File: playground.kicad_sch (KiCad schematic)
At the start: 47 parts, among them IC11 LM3940IMP-3.3_NOPB, IC9 L293DD, J1 67643-2910, J2 Pump, J3 Fan, J4 Valve, J5 Conn_02x05_Counter_Clockwise, J6 MOLEX POWER CONNECTOR, SW1 SW_DIP_x01, U2 ATSAMD21G18A-A, Y1 32.768kHz

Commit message: Updated layout and schem
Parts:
- removed C9: 1u, Capacitor_SMD:C_0805_2012Metric, symbol Device:C
- TP1, TP10, TP11, TP12, TP2, TP3, TP4, TP5, TP6, TP7, TP8, TP9: footprint TestPoint:TestPoint_Pad_D2.0mm -> TestPoint:TestPoint_Pad_D1.0mm
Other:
- note added: "ANA"
- note added: "CORE"
- note added: "IN"
- note added: "IO"
- moved on the sheet: C10, C11
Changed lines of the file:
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@@
 	)
 	(junction
+		(at 128.27 181.61)
+		(diameter 0)
+		(color 0 0 0 0)
+	)
+	(junction
 		(at 82.55 31.75)
 		(diameter 0)
@@
 	)
 	(junction
-		(at 128.27 181.61)
-		(diameter 0)
-		(color 0 0 0 0)
-	)
-	(junction
 		(at 161.29 133.35)
 		(diameter 0)
@@
 	)
 	(junction
+		(at 128.27 168.91)
+		(diameter 0)
+		(color 0 0 0 0)
+	)
+	(junction
 		(at 95.25 181.61)
 		(diameter 0)
@@
 	)
 	(junction
-		(at 138.43 168.91)
-		(diameter 0)
-		(color 0 0 0 0)
-	)
-	(junction
-		(at 138.43 181.61)
-		(diameter 0)
-		(color 0 0 0 0)
-	)
-	(junction
 		(at 49.53 52.07)
 		(diameter 0)
@@
 		(color 0 0 0 0)
 	)
-	(junction
-		(at 128.27 168.91)
-		(diameter 0)
-		(color 0 0 0 0)
-	)
 	(no_connect
 		(at 207.01 77.47)
@@
 	(wire
 		(pts
-			(xy 138.43 181.61) (xy 149.86 181.61)
+			(xy 128.27 181.61) (xy 139.7 181.61)
 		)
 		(stroke
@@
 	(wire
 		(pts
-			(xy 138.43 168.91) (xy 138.43 171.45)
+			(xy 128.27 168.91) (xy 128.27 171.45)
 		)
 		(stroke
@@
 	(wire
 		(pts
-			(xy 149.86 168.91) (xy 149.86 171.45)
+			(xy 139.7 168.91) (xy 139.7 171.45)
 		)
 		(stroke
@@
 	(wire
 		(pts
-			(xy 128.27 168.91) (xy 138.43 168.91)
-		)
-		(stroke
-			(width 0)
-			(type default)
-		)
-	)
-	(wire
-		(pts
 			(xy 118.11 168.91) (xy 128.27 168.91)
 		)
@@
 	(wire
 		(pts
-			(xy 128.27 181.61) (xy 138.43 181.61)
-		)
-		(stroke
-			(width 0)
-			(type default)
-		)
-	)
-	(wire
-		(pts
 			(xy 144.78 99.06) (xy 144.78 88.9)
 		)
@@
 	(wire
 		(pts
-			(xy 149.86 179.07) (xy 149.86 181.61)
+			(xy 139.7 179.07) (xy 139.7 181.61)
 		)
 		(stroke
@@
 	(wire
 		(pts
-			(xy 128.27 171.45) (xy 128.27 168.91)
-		)
-		(stroke
-			(width 0)
-			(type default)
-		)
-	)
-	(wire
-		(pts
 			(xy 143.51 36.83) (xy 146.05 36.83)
 		)
@@
 	(wire
 		(pts
-			(xy 138.43 179.07) (xy 138.43 181.61)
+			(xy 128.27 179.07) (xy 128.27 181.61)
 		)
 		(stroke
@@
 	(wire
 		(pts
-			(xy 128.27 179.07) (xy 128.27 181.61)
-		)
-		(stroke
-			(width 0)
-			(type default)
-		)
-	)
-	(wire
-		(pts
 			(xy 138.43 81.28) (xy 147.32 81.28)
 		)
@@
 	(wire
 		(pts
-			(xy 138.43 168.91) (xy 149.86 168.91)
+			(xy 128.27 168.91) (xy 139.7 168.91)
 		)
 		(stroke
@@
 		)
 	)
+	(text "IO"
+		(exclude_from_sim no)
+		(at 95.25 167.64 0)
+		(effects
+			(font
+				(size 1.27 1.27)
+			)
+		)
+	)
 	(text "Valve Controller"
 		(exclude_from_sim no)
@@
 		)
 	)
+	(text "ANA"
+		(exclude_from_sim no)
+		(at 139.192 167.132 0)
+		(effects
+			(font
+				(size 1.27 1.27)
+			)
+		)
+	)
 	(text "MOLEX POWER"
 		(exclude_from_sim no)
@@
 		)
 	)
+	(text "ANA"
+		(exclude_from_sim no)
+		(at 86.868 167.64 0)
+		(effects
+			(font
+				(size 1.27 1.27)
+			)
+		)
+	)
 	(text "(NOTE: might modify this)"
 		(exclude_from_sim no)
@@
 		)
 	)
+	(text "IN"
+		(exclude_from_sim no)
+		(at 106.68 167.386 0)
+		(effects
+			(font
+				(size 1.27 1.27)
+			)
+		)
+	)
 	(text "Level Shifter"
 		(exclude_from_sim no)
@@
 		)
 	)
+	(text "IN"
+		(exclude_from_sim no)
+		(at 128.27 167.132 0)
+		(effects
+			(font
+				(size 1.27 1.27)
+			)
+		)
+	)
+	(text "CORE"
+		(exclude_from_sim no)
+		(at 118.11 167.386 0)
+		(effects
+			(font
+				(size 1.27 1.27)
+			)
+		)
+	)
 	(label "SWDIO"
 		(at 25.4 168.91 0)
@@
 			)
 		)
-		(property "Footprint" "TestPoint:TestPoint_Pad_D2.0mm"
+		(property "Footprint" "TestPoint:TestPoint_Pad_D1.0mm"
 			(at 257.81 83.82 0)
 			(effects
@@
 			)
 		)
-		(property "Footprint" "TestPoint:TestPoint_Pad_D2.0mm"
+		(property "Footprint" "TestPoint:TestPoint_Pad_D1.0mm"
 			(at 255.27 62.23 0)
 			(effects
@@
 			)
 		)
-		(property "Footprint" "TestPoint:TestPoint_Pad_D2.0mm"
+		(property "Footprint" "TestPoint:TestPoint_Pad_D1.0mm"
 			(at 257.81 91.44 0)
 			(effects
@@
 			)
 		)
-		(property "Footprint" "TestPoint:TestPoint_Pad_D2.0mm"
+		(property "Footprint" "TestPoint:TestPoint_Pad_D1.0mm"
 			(at 257.81 78.74 0)
 			(effects
@@
 			)
 		)
-		(property "Footprint" "TestPoint:TestPoint_Pad_D2.0mm"
+		(property "Footprint" "TestPoint:TestPoint_Pad_D1.0mm"
 			(at 257.81 76.2 0)
 			(effects
@@
 			)
 		)
-		(property "Footprint" "TestPoint:TestPoint_Pad_D2.0mm"
+		(property "Footprint" "TestPoint:TestPoint_Pad_D1.0mm"
 			(at 257.81 93.98 0)
 			(effects
@@
 			)
 		)
-		(property "Footprint" "TestPoint:TestPoint_Pad_D2.0mm"
+		(property "Footprint" "TestPoint:TestPoint_Pad_D1.0mm"
 			(at 257.81 88.9 0)
 			(effects
@@
 			)
 		)
-		(property "Footprint" "TestPoint:TestPoint_Pad_D2.0mm"
+		(property "Footprint" "TestPoint:TestPoint_Pad_D1.0mm"
 			(at 247.65 62.23 0)
 			(effects
@@
 			)
 		)
-		(property "Footprint" "TestPoint:TestPoint_Pad_D2.0mm"
+		(property "Footprint" "TestPoint:TestPoint_Pad_D1.0mm"
 			(at 240.03 62.23 0)
 			(effects
@@
 	(symbol
 		(lib_id "Device:C")
-		(at 138.43 175.26 0)
+		(at 128.27 175.26 0)
 		(unit 1)
 		(exclude_from_sim no)
@@
 		(fields_autoplaced yes)
 		(property "Reference" "C10"
-			(at 142.24 173.9899 0)
+			(at 132.08 173.9899 0)
 			(effects
 				(font
@@
 		)
 		(property "Value" "10u"
-			(at 142.24 176.5299 0)
+			(at 132.08 176.5299 0)
 			(effects
 				(font
@@
 		)
 		(property "Footprint" "Capacitor_SMD:C_0805_2012Metric"
-			(at 139.3952 179.07 0)
+			(at 129.2352 179.07 0)
 			(effects
 				(font
@@
 		)
 		(property "Datasheet" "~"
-			(at 138.43 175.26 0)
+			(at 128.27 175.26 0)
 			(effects
 				(font
@@
 		)
 		(property "Description" "Unpolarized capacitor"
-			(at 138.43 175.26 0)
+			(at 128.27 175.26 0)
 			(effects
 				(font
@@
 	(symbol
 		(lib_id "Device:C")
-		(at 149.86 175.26 0)
+		(at 139.7 175.26 0)
 		(unit 1)
 		(exclude_from_sim no)
@@
 		(fields_autoplaced yes)
 		(property "Reference" "C11"
-			(at 153.67 173.9899 0)
+			(at 143.51 173.9899 0)
 			(effects
 				(font
@@
 		)
 		(property "Value" "10u"
-			(at 153.67 176.5299 0)
+			(at 143.51 176.5299 0)
 			(effects
 				(font
@@
 		)
 		(property "Footprint" "Capacitor_SMD:C_0805_2012Metric"
-			(at 150.8252 179.07 0)
+			(at 140.6652 179.07 0)
 			(effects
 				(font
@@
 		)
 		(property "Datasheet" "~"
-			(at 149.86 175.26 0)
+			(at 139.7 175.26 0)
 			(effects
 				(font
@@
 		)
 		(property "Description" "Unpolarized capacitor"
-			(at 149.86 175.26 0)
+			(at 139.7 175.26 0)
 			(effects
 				(font
@@
 	)
 	(symbol
-		(lib_id "Device:C")
-		(at 128.27 175.26 0)
-		(unit 1)
-		(exclude_from_sim no)
-		(in_bom yes)
-		(on_board yes)
-		(dnp no)
-		(fields_autoplaced yes)
-		(property "Reference" "C9"
-			(at 132.08 173.9899 0)
-			(effects
-				(font
-					(size 1.27 1.27)
-				)
-				(justify left)
-			)
-		)
-		(property "Value" "1u"
-			(at 132.08 176.5299 0)
-			(effects
-				(font
-					(size 1.27 1.27)
-				)
-				(justify left)
-			)
-		)
-		(property "Footprint" "Capacitor_SMD:C_0805_2012Metric"
-			(at 129.2352 179.07 0)
-			(effects
-				(font
-					(size 1.27 1.27)
-				)
-				(hide yes)
-			)
-		)
-		(property "Datasheet" "~"
-			(at 128.27 175.26 0)
-			(effects
-				(font
-					(size 1.27 1.27)
-				)
-				(hide yes)
-			)
-		)
-		(property "Description" "Unpolarized capacitor"
-			(at 128.27 175.26 0)
-			(effects
-				(font
-					(size 1.27 1.27)
-				)
-				(hide yes)
-			)
-		)
-		(pin "1"
-		)
-		(pin "2"
-		)
-		(instances
-			(project "playground"
-				(path "/e7dc7c2b-347f-4a52-91f1-4651868a2780"
-					(reference "C9")
-					(unit 1)
-				)
-			)
-		)
-	)
-	(symbol
 		(lib_id "power:+3V3")
 		(at 83.82 168.91 0)
@@
 			)
 		)
-		(property "Footprint" "TestPoint:TestPoint_Pad_D2.0mm"
+		(property "Footprint" "TestPoint:TestPoint_Pad_D1.0mm"
 			(at 262.89 62.23 0)
 			(effects
@@
 			)
 		)
-		(property "Footprint" "TestPoint:TestPoint_Pad_D2.0mm"
+		(property "Footprint" "TestPoint:TestPoint_Pad_D1.0mm"
 			(at 257.81 86.36 0)
 			(effects
@@
 			)
 		)
-		(property "Footprint" "TestPoint:TestPoint_Pad_D2.0mm"
+		(property "Footprint" "TestPoint:TestPoint_Pad_D1.0mm"
 			(at 257.81 81.28 0)
 			(effects

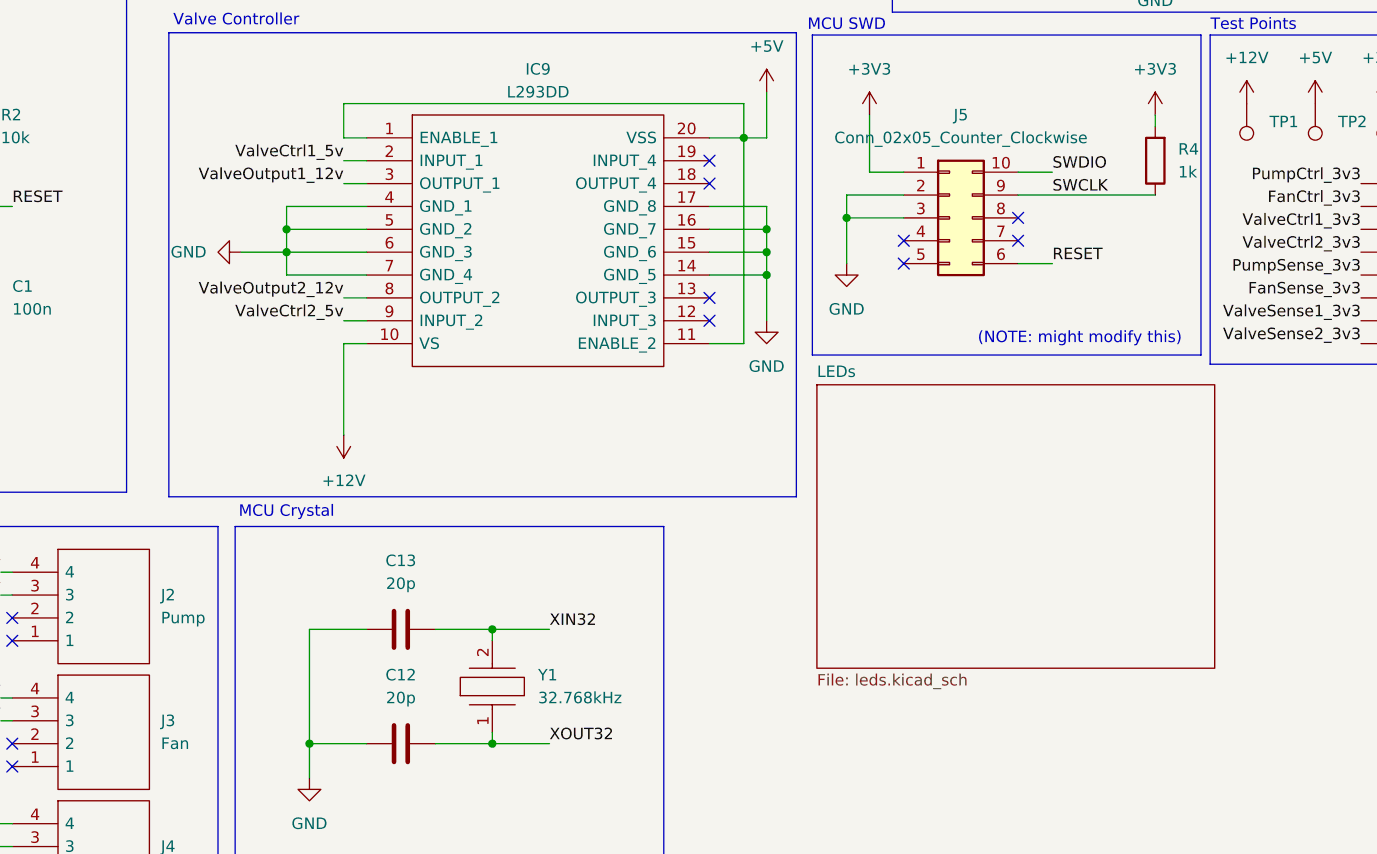
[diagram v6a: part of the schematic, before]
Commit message: Layout of indicator LEDs. Shrank design space
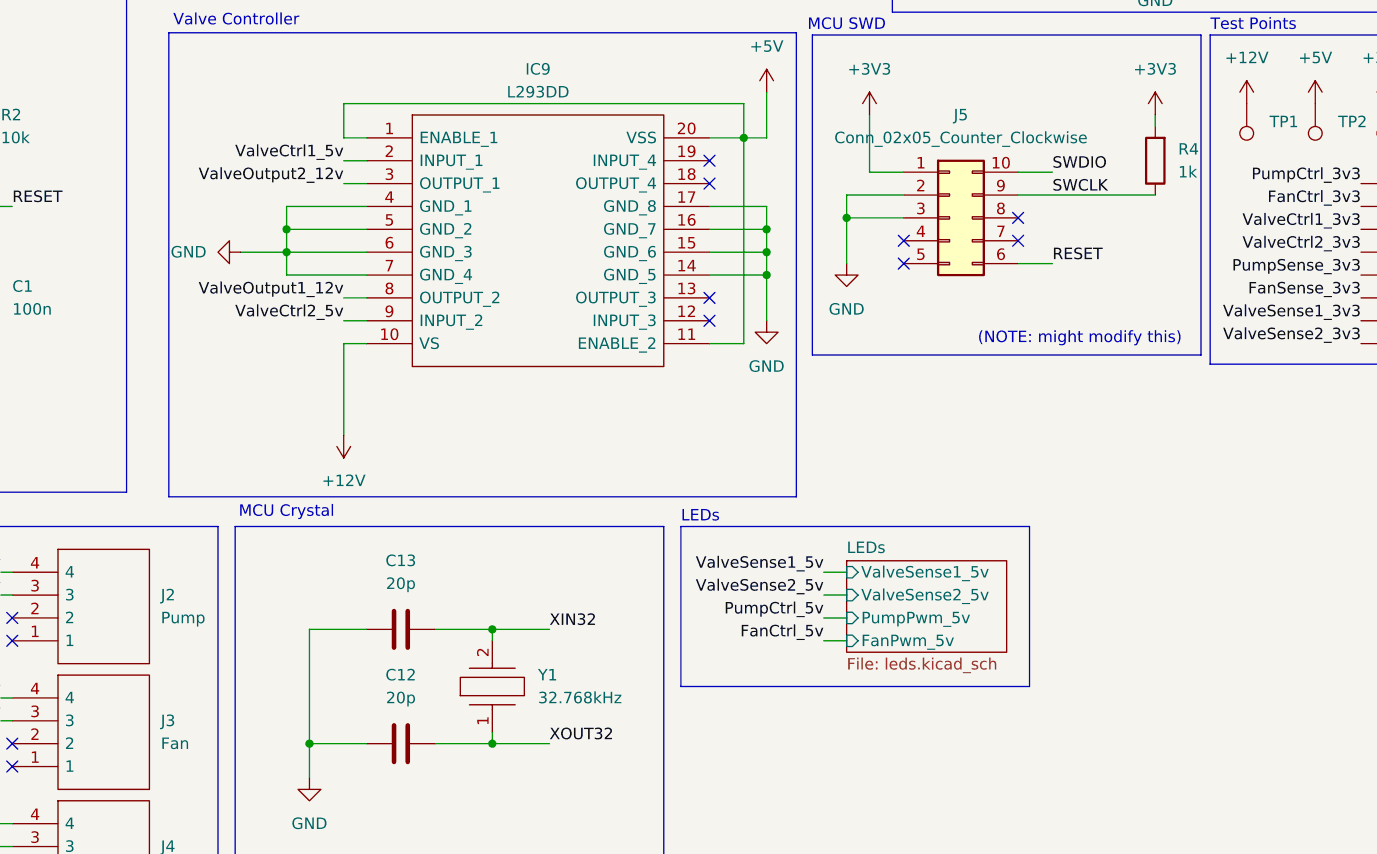
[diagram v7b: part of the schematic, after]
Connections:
- net ValveOutput1_12v: now also IC9.8 (OUTPUT_2); no longer IC9.3 (OUTPUT_1)
- net ValveOutput2_12v: now also IC9.3 (OUTPUT_1); no longer IC9.8 (OUTPUT_2)
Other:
- sheet LEDs ports: added FanPwm_5v, PumpPwm_5v, ValveSense1_5v, ValveSense2_5v; removed none
- note added: "LEDs"
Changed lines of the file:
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@@
 	(wire
 		(pts
+			(xy 198.12 114.3) (xy 200.66 114.3)
+		)
+		(stroke
+			(width 0)
+			(type default)
+		)
+	)
+	(wire
+		(pts
 			(xy 105.41 147.32) (xy 107.95 147.32)
 		)
@@
 	(wire
 		(pts
+			(xy 198.12 116.84) (xy 200.66 116.84)
+		)
+		(stroke
+			(width 0)
+			(type default)
+		)
+	)
+	(wire
+		(pts
 			(xy 17.78 173.99) (xy 35.56 173.99)
 		)
@@
 	(wire
 		(pts
+			(xy 198.12 121.92) (xy 200.66 121.92)
+		)
+		(stroke
+			(width 0)
+			(type default)
+		)
+	)
+	(wire
+		(pts
 			(xy 106.68 130.81) (xy 107.95 130.81)
 		)
@@
 	(wire
 		(pts
+			(xy 198.12 119.38) (xy 200.66 119.38)
+		)
+		(stroke
+			(width 0)
+			(type default)
+		)
+	)
+	(wire
+		(pts
 			(xy 144.78 68.58) (xy 147.32 68.58)
 		)
@@
 	)
 	(rectangle
+		(start 182.245 109.22)
+		(end 220.98 127)
+		(stroke
+			(width 0)
+			(type default)
+		)
+		(fill
+			(type none)
+		)
+	)
+	(rectangle
 		(start 125.476 15.748)
 		(end 204.216 49.784)
@@
 		)
 	)
+	(text "LEDs"
+		(exclude_from_sim no)
+		(at 184.404 108.204 0)
+		(effects
+			(font
+				(size 1.27 1.27)
+			)
+		)
+	)
 	(text "Valve Controller"
 		(exclude_from_sim no)
@@
 		)
 	)
+	(label "ValveSense2_5v"
+		(at 198.12 116.84 180)
+		(fields_autoplaced yes)
+		(effects
+			(font
+				(size 1.27 1.27)
+			)
+			(justify right bottom)
+		)
+	)
 	(label "USB_D+"
 		(at 68.58 39.37 0)
@@
 		)
 	)
+	(label "PumpCtrl_5v"
+		(at 198.12 119.38 180)
+		(fields_autoplaced yes)
+		(effects
+			(font
+				(size 1.27 1.27)
+			)
+			(justify right bottom)
+		)
+	)
 	(label "ValveSense2_5v"
 		(at 105.41 149.86 180)
@@
 		)
 	)
+	(label "ValveSense1_5v"
+		(at 198.12 114.3 180)
+		(fields_autoplaced yes)
+		(effects
+			(font
+				(size 1.27 1.27)
+			)
+			(justify right bottom)
+		)
+	)
 	(label "XIN32"
 		(at 24.13 90.17 0)
@@
 	)
 	(label "ValveOutput2_12v"
-		(at 144.78 83.82 180)
+		(at 144.78 71.12 180)
 		(fields_autoplaced yes)
 		(effects
@@
 		)
 	)
+	(label "FanCtrl_5v"
+		(at 198.12 121.92 180)
+		(fields_autoplaced yes)
+		(effects
+			(font
+				(size 1.27 1.27)
+			)
+			(justify right bottom)
+		)
+	)
 	(label "ValveOutput1_12v"
-		(at 144.78 71.12 180)
+		(at 144.78 83.82 180)
 		(fields_autoplaced yes)
 		(effects
@@
 	)
 	(sheet
-		(at 197.358 93.472)
-		(size 44.196 31.496)
+		(at 200.66 113.03)
+		(size 17.78 10.16)
 		(fields_autoplaced yes)
 		(stroke
@@
 		)
 		(property "Sheetname" "LEDs"
-			(at 197.358 92.7604 0)
+			(at 200.66 112.3184 0)
 			(effects
 				(font
@@
 		)
 		(property "Sheetfile" "leds.kicad_sch"
-			(at 197.358 125.5526 0)
+			(at 200.66 123.7746 0)
 			(effects
 				(font
@@
 			)
 		)
+		(pin "ValveSense1_5v" input
+			(at 200.66 114.3 180)
+			(effects
+				(font
+					(size 1.27 1.27)
+				)
+				(justify left)
+			)
+		)
+		(pin "ValveSense2_5v" input
+			(at 200.66 116.84 180)
+			(effects
+				(font
+					(size 1.27 1.27)
+				)
+				(justify left)
+			)
+		)
+		(pin "PumpPwm_5v" input
+			(at 200.66 119.38 180)
+			(effects
+				(font
+					(size 1.27 1.27)
+				)
+				(justify left)
+			)
+		)
+		(pin "FanPwm_5v" input
+			(at 200.66 121.92 180)
+			(effects
+				(font
+					(size 1.27 1.27)
+				)
+				(justify left)
+			)
+		)

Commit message: Initial Layout
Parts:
- added H1, H2, H3, H4: MountingHole_Pad, MountingHole:MountingHole_2.2mm_M2_Pad, symbol Mechanical:MountingHole_Pad
- J5: footprint Connector_PinHeader_2.54mm:PinHeader_2x05_P2.54mm_Vertical_SMD -> Connector_PinHeader_2.54mm:PinHeader_2x05_P2.54mm_Vertical
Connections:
- net GND: now also H1.1, H2.1, H3.1, H4.1
- net RST_SW_R: now reaches R1.1, SW1.1
